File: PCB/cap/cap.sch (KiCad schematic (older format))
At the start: 21 parts, among them J1 Servo1, J2 Servo2, J3 LS1, J4 LS2, J5 VCC/GND-IN, J6 Radio, J7 FSR1, J8 FSR2, Q1 Q_PMOS_DGS, U1 ACS723xLCTR-05AB

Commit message: Minor updates to PCB. Push to windows.
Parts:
- removed J2: Servo2, Connector_PinSocket_2.54mm:PinSocket_1x03_P2.54mm_Vertical, symbol Connector_Generic:Conn_01x03
- removed J8: FSR2, Connector_PinHeader_2.54mm:PinHeader_1x02_P2.54mm_Vertical, symbol Connector_Generic:Conn_01x02
- removed Q1: Q_PMOS_DGS, Package_TO_SOT_SMD:SOT-23, symbol Device:Q_PMOS_DGS
- removed R5: 10k, Resistor_SMD:R_0603_1608Metric, symbol Device:R
- added U2: NRF24L01_Breakout, RF_Module:nRF24L01_Breakout, symbol RF:NRF24L01_Breakout
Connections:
- net labels removed: A2
- wire segments 89 -> 75
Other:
- note added: "FSR"
- note added: "Mounting holes on board\nDoes the RC need capacitor across power? Switch on VCC?\nScrew terminal FSR footprint?\nMeasure new servos and then select a unit with correct full scale range. -> voltage divider\nMounting holes\nComponent size and BOM?"
- note added: "Servo"
- note removed: "FSR’s"
- note removed: "Mounting holes on board\nDoes the RC need capacitor across power? Switch on VCC?\nScrew terminal FSR footprint?\nMeasure new servos and then select a unit with correct full scale range. -> voltage divider"
- note removed: "Servos"
- moved on the sheet: D1, D2, J1, J3, J4, J7, R1, R2, R4

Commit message: Added two current sensing options. Hall and shunt
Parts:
- removed D2: R-LED, LED_SMD:LED_0603_1608Metric, symbol Device:LED
- removed R1: 140, Resistor_SMD:R_0603_1608Metric, symbol Device:R
- removed U1: ACS723xLCTR-05AB, Package_SO:SOIC-8_3.9x4.9mm_P1.27mm, symbol Sensor_Current:ACS723xLCTR-05AB
- added C?: 0.1 uF, Capacitor_SMD:C_0603_1608Metric, symbol Device:C
- added D?: G-LED, LED_SMD:LED_1206_3216Metric_Pad1.42x1.75mm_HandSolder, symbol Device:LED
- added H? (x2): MountingHole_Pad, MountingHole:MountingHole_3.2mm_M3_ISO14580_Pad, symbol Mechanical:MountingHole_Pad
- added R?: 140, Resistor_SMD:R_1206_3216Metric_Pad1.42x1.75mm_HandSolder, symbol Device:R
- added R?: 16 mOhm, Resistor_SMD:R_2512_6332Metric_Pad1.52x3.35mm_HandSolder, symbol Device:R
- added U?: INA181A3, Package_TO_SOT_SMD:SOT-23-6, symbol Amplifier_Current:INA181
- added U?: ACS723xLCTR-05AB, Package_SO:SOIC-8_3.9x4.9mm_P1.27mm, symbol Sensor_Current:ACS723xLCTR-05AB
- A1: Link (none) -> https://www.amazon.ca/gp/product/B01N7I0W77/ref=ppx_od_dt_b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
- D1: footprint LED_SMD:LED_0603_1608Metric -> LED_SMD:LED_1206_3216Metric_Pad1.42x1.75mm_HandSolder
- R2: footprint Resistor_SMD:R_0603_1608Metric -> Resistor_SMD:R_1206_3216Metric_Pad1.42x1.75mm_HandSolder
- R3: value 5.1K -> 5.1 kOhm
- U2: Link (none) -> https://www.amazon.ca/gp/product/B01C3YNGI8/ref=ppx_yo_dt_b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
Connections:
- net +5V: now also C?.1, U?.6 (V+), U?.8 (VCC)
- net A1: now also U?.7 (VIOUT)
- net BW_SEL: now also U?.6 (BW_SEL)
- net D9: now also R?.1
- net GND: now also C?.2, D?.1 (K), H?.1, H?.1, U?.2 (GND), U?.5 (GND), U?.5 (REF)
- net VCC: now also U?.1 (IP+), U?.2 (IP+); no longer J1.2 (Pin_2)
- net A2: now reaches A1.21 (A2)
- net A2: now also U?.1
- net at R2.2: now also D?.2 (A)
- net at D1.2 (A): now also R?.2
- new net Vdrive: J1.2 (Pin_2), R?.1, R?.2, U?.3 (+), U?.3 (IP-), U?.4 (-), U?.4 (IP-)
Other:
- note added: "Current Sensor A"
- note added: "Current Sensor B"
- note added: "Mounting holes on board\nDoes the RC need capacitor across power? Switch on VCC?\nScrew terminal FSR footprint?\nMeasure new servos and then select a unit with correct full scale range. -> voltage divider\nMounting holes\nComponent size and BOM?\nShield for odroid or whatever?"
- note added: "Open 20 kHz\nClose 80 kHz"
- note removed: "Current Sensor"
- note removed: "Mounting holes on board\nDoes the RC need capacitor across power? Switch on VCC?\nScrew terminal FSR footprint?\nMeasure new servos and then select a unit with correct full scale range. -> voltage divider\nMounting holes\nComponent size and BOM?"
- moved on the sheet: C1, C2, D1, J6, J7, JP1, R2, R3, R4, U2

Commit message: Conceptual schematic completed
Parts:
- removed J6: Radio, Connector_PinHeader_2.54mm:PinHeader_2x04_P2.54mm_Vertical, symbol Connector_Generic:Conn_02x04_Top_Bottom
- added H3, H4: MountingHole_Pad, MountingHole:MountingHole_3.2mm_M3_ISO14580_Pad, symbol Mechanical:MountingHole_Pad
- D1: footprint LED_SMD:LED_1206_3216Metric_Pad1.42x1.75mm_HandSolder -> LED_SMD:LED_0603_1608Metric_Pad1.05x0.95mm_HandSolder
- D2: renamed from D?; footprint LED_SMD:LED_1206_3216Metric_Pad1.42x1.75mm_HandSolder -> LED_SMD:LED_0603_1608Metric_Pad1.05x0.95mm_HandSolder
- R2: value 140 -> -; footprint Resistor_SMD:R_1206_3216Metric_Pad1.42x1.75mm_HandSolder -> Resistor_SMD:R_0603_1608Metric_Pad1.05x0.95mm_HandSolder
- R4: value 10k -> 10 kOhm
- R5: renamed from R?; value 140 -> -; footprint Resistor_SMD:R_1206_3216Metric_Pad1.42x1.75mm_HandSolder -> Resistor_SMD:R_0603_1608Metric_Pad1.05x0.95mm_HandSolder
- gave numbers to parts that had none: 6
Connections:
- net +3V3: now also U2.2 (VCC)
- net CE: now also U2.3 (CE)
- net CSN: now also U2.4 (~CSN)
- net GND: now also U2.1 (GND), H3.1, H4.1
- net MISO: now also U2.7 (MISO)
- net MOSI: now also U2.6 (MOSI)
- net SCK: now also U2.5 (SCK)
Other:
- note added: "Communication"
- note added: "Force Sensitive Resistor (FSR)"
- note added: "Microcontroller"
- note added: "Power in"
- note added: "Screw terminal FSR footprint?\nDouble check / create BOM\nShield for odroid or whatever?"
- note added: "Servo Out"
- note removed: "FSR"
- note removed: "Indicator LEDs"
- note removed: "Mounting holes on board\nDoes the RC need capacitor across power? Switch on VCC?\nScrew terminal FSR footprint?\nMeasure new servos and then select a unit with correct full scale range. -> voltage divider\nMounting holes\nComponent size and BOM?\nShield for odroid or whatever?"
- note removed: "Power In"
- note removed: "Radio"
- note removed: "Servo"
- moved on the sheet: A1, H1, H2, J1, J4, J5, J7, R4, U2

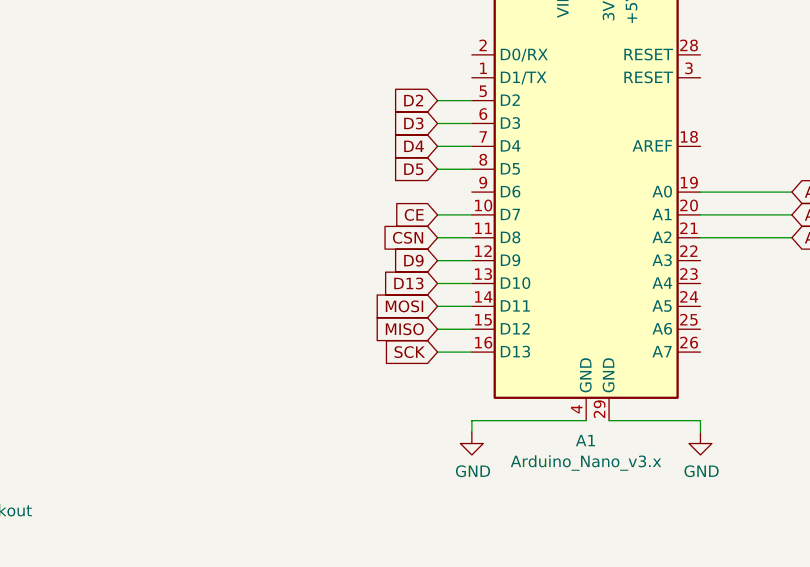
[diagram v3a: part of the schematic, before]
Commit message: Layed out mjaor components, need to select connectors.
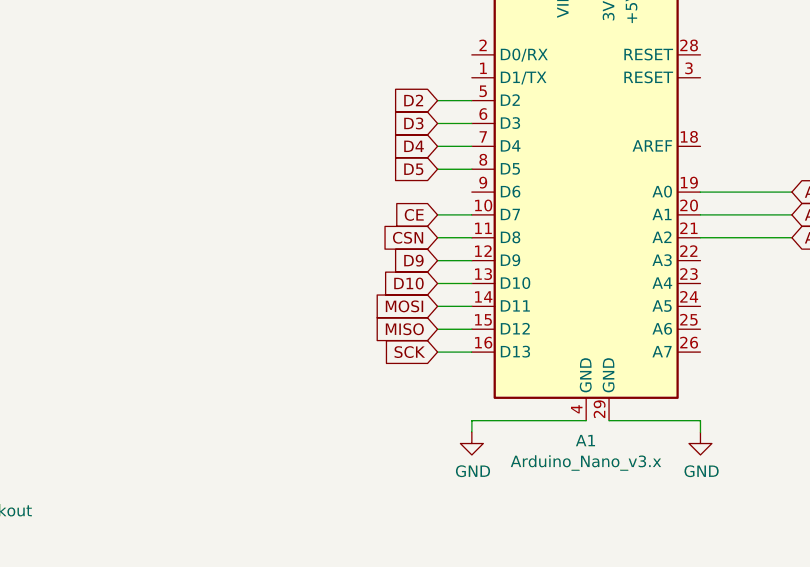
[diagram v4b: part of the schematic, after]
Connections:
- net D13 is gone; now on net D10: A1.13 (D10)
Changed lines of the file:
@@
 D9
 Text GLabel 4700 4750 0    50   Input ~ 0
-D13
+D10
 Text GLabel 1100 6900 0    50   Input ~ 0
 D9
@@
 $EndComp
 $Comp
-L power:+3.3V #PWR?
+L power:+3.3V #PWR0111
 U 1 1 5EB91A5C
 P 1850 5050
-F 0 "#PWR?" H 1850 4900 50  0001 C CNN
+F 0 "#PWR0111" H 1850 4900 50  0001 C CNN
 F 1 "+3.3V" H 1865 5223 50  0000 C CNN
 F 2 "" H 1850 5050 50  0001 C CNN

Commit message: Added Molex connectors and conceptual layout complete
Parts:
- A1: symbol MCU_Module:Arduino_Nano_v3.x -> cap-rescue:Arduino_Nano_v3.x-MCU_Module
- J1: footprint Connector_PinSocket_2.54mm:PinSocket_1x03_P2.54mm_Vertical -> Connector_Molex:Molex_Micro-Fit_3.0_43650-0300_1x03_P3.00mm_Horizontal
- J3, J4, J5: footprint Connector_PinSocket_2.54mm:PinSocket_1x02_P2.54mm_Vertical -> Connector_Molex:Molex_Micro-Fit_3.0_43650-0200_1x02_P3.00mm_Horizontal
- J7: footprint Connector_PinHeader_2.54mm:PinHeader_1x02_P2.54mm_Vertical -> Connector_Molex:Molex_Micro-Fit_3.0_43650-0200_1x02_P3.00mm_Horizontal
- R1: footprint Resistor_SMD:R_2512_6332Metric_Pad1.52x3.35mm_HandSolder -> Resistor_SMD:R_1206_3216Metric_Pad1.42x1.75mm_HandSolder; Field4 A109675CT-ND -> P0.016BVCT-ND
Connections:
- net +5V: now also J7.2 (Pin_2); no longer J7.1 (Pin_1)
- net A0: now also J7.1 (Pin_1); no longer J7.2 (Pin_2)
- net D2: now also J3.2 (Pin_2); no longer J3.1 (Pin_1)
- net D3: now also J4.2 (Pin_2); no longer J4.1 (Pin_1)
- net D4: now also J1.3 (Pin_3); no longer J1.1 (Pin_1)
- net GND: now also J1.1 (Pin_1), J3.1 (Pin_1), J4.1 (Pin_1); no longer J1.3 (Pin_3), J3.2 (Pin_2), J4.2 (Pin_2)
- net Vdrive: no longer R1.2, U1.3 (IP-), U1.4 (IP-), U3.3 (+)
- net A6: now reaches A1.25 (A6)
- net A6: now also C1.1, U1.7 (VIOUT)
- removed net A1: A1.20 (A1), C1.1, U1.7 (VIOUT)
- new net VDD: R1.2, U1.3 (IP-), U1.4 (IP-), U3.3 (+)
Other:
- note removed: "Screw terminal FSR footprint?\nDouble check / create BOM\nShield for odroid or whatever?"
- moved on the sheet: J1, J3, J4, J5, J7, R4

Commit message: Board routed.
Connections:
- net D2: now also J4.2 (Pin_2); no longer J3.2 (Pin_2)
- net D3: now also J3.2 (Pin_2); no longer J4.2 (Pin_2)
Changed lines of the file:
@@
 EESchema Schematic File Version 4
+LIBS:cap-cache
 EELAYER 30 0
 EELAYER END
@@
 	-1   0    0    -1
 $EndComp
+Text GLabel 1350 1050 0    50   Input ~ 0
+D3
 Text GLabel 1350 1550 0    50   Input ~ 0
-D3
-Text GLabel 1350 1050 0    50   Input ~ 0
 D2
 $Comp

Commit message: All schematics detail check complete
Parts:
- C2, C3: Field4 (none) -> 399-7845-1-ND
- D1: value G-LED -> R-LED; Field4 (none) -> 160-1447-1-ND
- D2: Field4 (none) -> 160-1443-6-ND
- R2, R5: value - -> 220 ohm; Field4 (none) -> P220BZCT-ND
- R4: Field4 (none) -> P10.0KHCT-ND
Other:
- note added: "Indicators"
- note added: "Mounting"
- note added: "RF Communication"
- note removed: "Communication"
- moved on the sheet: J1, J3, J4, J5, J7, R4, U2
